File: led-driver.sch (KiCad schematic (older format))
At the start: 18 parts, among them J1 48VDC IN, J2 ENABLE, J3 ADJ, J4 LED, Q1 ZXMP7A17KTC, U1 LM3409HV

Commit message: Rescue symbols, minor revisions to PCB
This commits previous work that took place sporadically between the last
commit a year and a half ago, and now.
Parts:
- C1, C2, C3, C4, C5: symbol C_Small -> led-driver-rescue:C_Small
- D1: symbol D_Schottky_Small_ALT -> led-driver-rescue:D_Schottky_Small_ALT
- J1, J3, J4: symbol CONN_01X02 -> led-driver-rescue:CONN_01X02
- J2: symbol CONN_01X03 -> led-driver-rescue:CONN_01X03
- L1: symbol L_Small -> led-driver-rescue:L_Small
- Q1: symbol Q_PMOS_GDS -> led-driver-rescue:Q_PMOS_GDS
- R1, R2, R3, R4, R5: symbol R_Small -> led-driver-rescue:R_Small
- U1: symbol LM3409-RESCUE-led-driver-new -> led-driver-rescue:LM3409-RESCUE-led-driver-new
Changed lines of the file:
@@
-EESchema Schematic File Version 2
-LIBS:led-driver
-EELAYER 25 0
+EESchema Schematic File Version 4
+LIBS:led-driver-cache
+EELAYER 29 0
 EELAYER END
 $Descr A4 11693 8268
@@
 $EndDescr
 $Comp
-L R_Small R4
+L led-driver-rescue:R_Small R4
 U 1 1 59AE9865
 P 5800 3300
@@
 $EndComp
 $Comp
-L D_Schottky_Small_ALT D1
+L led-driver-rescue:D_Schottky_Small_ALT D1
 U 1 1 59AE99D5
 P 5800 4000
@@
 $EndComp
 $Comp
-L L_Small L1
+L led-driver-rescue:L_Small L1
 U 1 1 59AE9B0A
 P 6050 3850
@@
 $EndComp
 $Comp
-L C_Small C3
+L led-driver-rescue:C_Small C3
 U 1 1 59AE9DC4
 P 5650 2900
@@
 $EndComp
 $Comp
-L C_Small C1
+L led-driver-rescue:C_Small C1
 U 1 1 59AE9F39
 P 2300 3100
@@
 $EndComp
 $Comp
-L GND #PWR01
+L led-driver-rescue:GND #PWR01
 U 1 1 59AEA1C1
 P 5800 4100
@@
 $EndComp
 $Comp
-L CONN_01X02 J4
+L led-driver-rescue:CONN_01X02 J4
 U 1 1 59AEA206
 P 6950 3900
@@
 $EndComp
 $Comp
-L GND #PWR02
+L led-driver-rescue:GND #PWR02
 U 1 1 59AEA35C
 P 6750 4100
@@
 $EndComp
 $Comp
-L GND #PWR03
+L led-driver-rescue:GND #PWR03
 U 1 1 59AEA3BF
 P 4350 3750
@@
 $EndComp
 $Comp
-L C_Small C2
+L led-driver-rescue:C_Small C2
 U 1 1 59AEA43B
 P 4250 4100
@@
 $EndComp
 $Comp
-L R_Small R1
+L led-driver-rescue:R_Small R1
 U 1 1 59AEA5E2
 P 4550 4000
@@
 $EndComp
 $Comp
-L GND #PWR04
+L led-driver-rescue:GND #PWR04
 U 1 1 59AEA82C
 P 4250 4200
@@
 $EndComp
 $Comp
-L GND #PWR05
+L led-driver-rescue:GND #PWR05
 U 1 1 59AEABBE
 P 2300 3200
@@
 $EndComp
 $Comp
-L CONN_01X02 J1
+L led-driver-rescue:CONN_01X02 J1
 U 1 1 59AEAC70
 P 1900 3050
@@
 $EndComp
 $Comp
-L R_Small R3
+L led-driver-rescue:R_Small R3
 U 1 1 59AEAE7C
 P 4100 2500
@@
 $EndComp
 $Comp
-L R_Small R2
+L led-driver-rescue:R_Small R2
 U 1 1 59AEAEBF
 P 4100 2700
@@
 $EndComp
 $Comp
-L VCC #PWR06
+L led-driver-rescue:VCC #PWR06
 U 1 1 59AEAF69
 P 4100 2400
@@
 $EndComp
 $Comp
-L VCC #PWR07
+L led-driver-rescue:VCC #PWR07
 U 1 1 59AEAFA4
 P 5800 3200
@@
 $EndComp
 $Comp
-L VCC #PWR08
+L led-driver-rescue:VCC #PWR08
 U 1 1 59AEB027
 P 5650 2800
@@
 $EndComp
 $Comp
-L VCC #PWR09
+L led-driver-rescue:VCC #PWR09
 U 1 1 59AEB4E1
 P 2100 3000
@@
 $EndComp
 $Comp
-L GND #PWR010
+L led-driver-rescue:GND #PWR010
 U 1 1 59AEB7E3
 P 4100 2800
@@
 $EndComp
 $Comp
-L VCC #PWR011
+L led-driver-rescue:VCC #PWR011
 U 1 1 59AEBCD0
 P 3700 3500
@@
 $EndComp
 $Comp
-L GND #PWR012
+L led-driver-rescue:GND #PWR012
 U 1 1 59AEC65E
 P 3500 3100
@@
 $EndComp
 $Comp
-L CONN_01X02 J3
+L led-driver-rescue:CONN_01X02 J3
 U 1 1 59AEC9E5
 P 3300 3050
@@
 $EndComp
 $Comp
-L CONN_01X03 J2
+L led-driver-rescue:CONN_01X03 J2
 U 1 1 59AED2EC
 P 3500 3600
@@
 $EndComp
 $Comp
-L GND #PWR013
+L led-driver-rescue:GND #PWR013
 U 1 1 59AED340
 P 3700 3700
@@
 $EndComp
 $Comp
-L LM3409-RESCUE-led-driver-new U1
+L led-driver-rescue:LM3409-RESCUE-led-driver-new U1
 U 1 1 59AEF993
 P 4900 3200
@@
 $EndComp
 Wire Wire Line
-	5800 3800 5800 3900
+	5800 3800 5800 3850
 Wire Wire Line
 	5800 3850 5950 3850
@@
 	5500 3000 5650 3000
 Wire Wire Line
-	6150 3850 6750 3850
+	6150 3850 6250 3850
 Wire Wire Line
 	6750 4100 6750 3950
@@
 	4300 2600 4300 2800
 Wire Wire Line
-	3500 3000 4300 3000
-$Comp
-L C_Small C4
+	3500 3000 3900 3000
+$Comp
+L led-driver-rescue:C_Small C4
 U 1 1 59AF72EA
 P 3900 3100
@@
 $EndComp
 $Comp
-L GND #PWR014
+L led-driver-rescue:GND #PWR014
 U 1 1 59AF7850
 P 3900 3200
@@
 Connection ~ 3900 3000
 $Comp
-L C_Small C5
+L led-driver-rescue:C_Small C5
 U 1 1 59AFE85B
 P 6400 3950
@@
 $EndComp
 $Comp
-L GND #PWR015
+L led-driver-rescue:GND #PWR015
 U 1 1 59AFEC38
 P 6400 4050
@@
 	4650 4300 6250 4300
 $Comp
-L GND #PWR016
+L led-driver-rescue:GND #PWR016
 U 1 1 59B109B8
 P 4900 3900
@@
 $EndComp
 $Comp
-L R_Small R5
+L led-driver-rescue:R_Small R5
 U 1 1 59B11505
 P 6200 3300
@@
 Connection ~ 5800 3400
 $Comp
-L Q_PMOS_GDS Q1
+L led-driver-rescue:Q_PMOS_GDS Q1
 U 1 1 59B006E4
 P 5700 3600
@@
 $EndComp
 Wire Wire Line
-	5500 3200 6200 3200
-Wire Wire Line
-	5500 3400 6200 3400
+	5500 3200 5800 3200
+Wire Wire Line
+	5500 3400 5800 3400
+Wire Wire Line
+	5800 3850 5800 3900
+Wire Wire Line
+	3900 3000 4300 3000
+Wire Wire Line
+	6400 3850 6750 3850
+Wire Wire Line
+	5800 3200 6200 3200
+Wire Wire Line
+	5800 3400 6200 3400
 $EndSCHEMATC

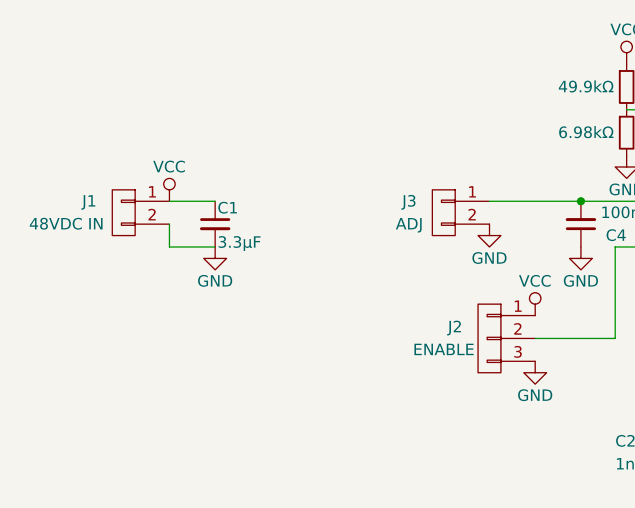
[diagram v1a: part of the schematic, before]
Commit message: Add PWR_FLAGs to power input
This quells warnings about connected-but-not-driven nets for GND and VCC
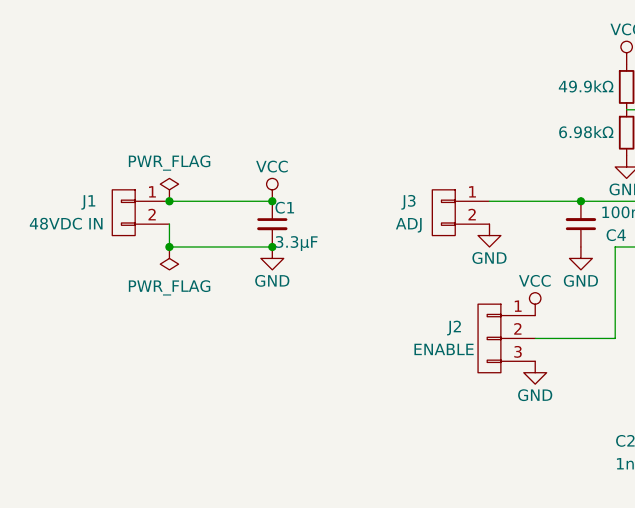
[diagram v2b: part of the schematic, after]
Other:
- moved on the sheet: C1

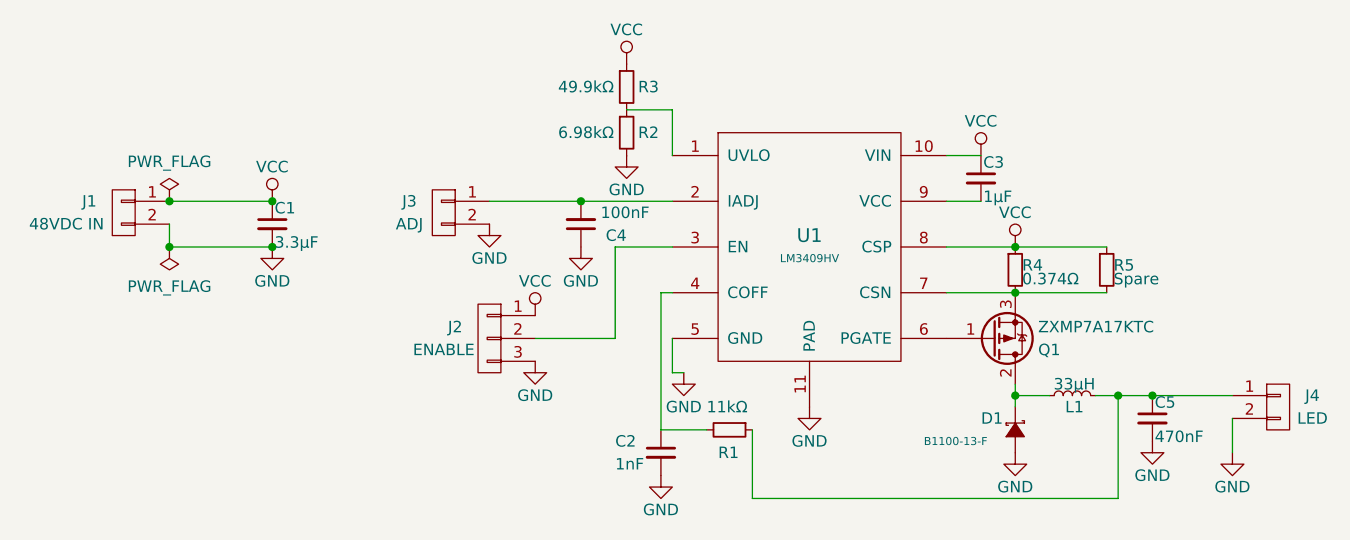
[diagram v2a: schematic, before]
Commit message: Increase UVLO turn-on to 43 V
The initial design assumed that the UVLO was a feature of the LM3409 not needed
by this board. It was set at the datasheet values of 10.1 V turn-on with 1.1 V
of hysteresis. However, during testing, I have found that the supply will sink
a maximum of around 600 mA into the load when operated into dropout. The LM3409
datasheet confirms that this is expected behaviour. Since the supply is
designed for LEDs modules with a forward voltage of 37 V, this patch changes
the UVLO to just over 43 volts, meaning that we do not run the LEDs above the
supply's design current of 450 mA.
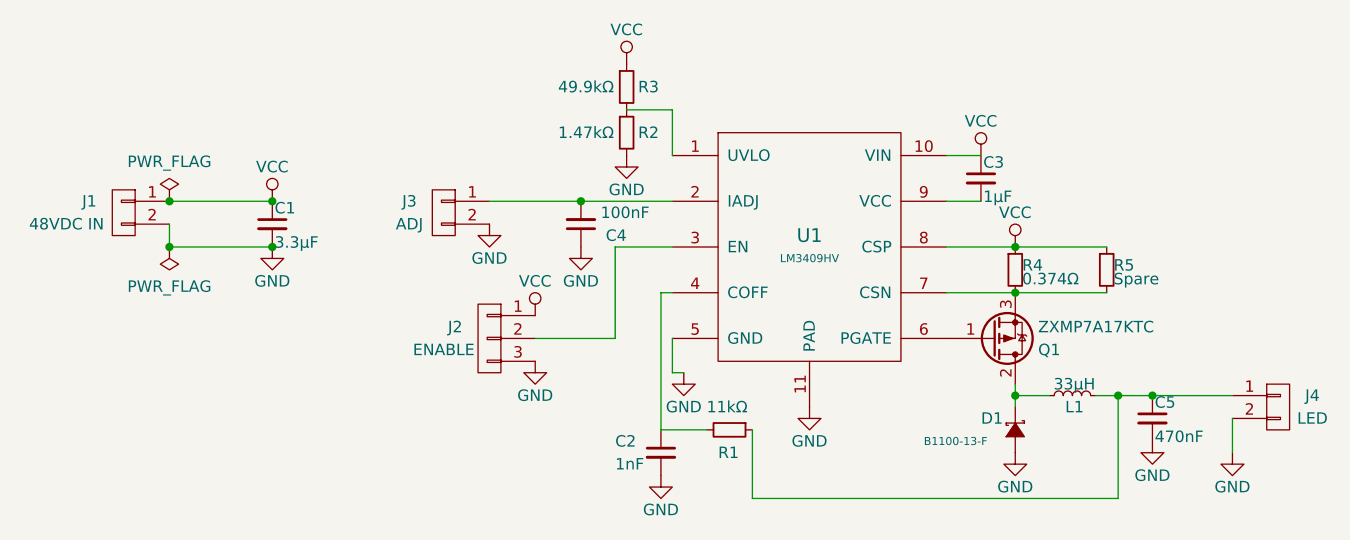
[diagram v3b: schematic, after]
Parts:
- R2: value 6.98kΩ -> 1.47kΩ
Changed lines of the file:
@@
 P 4100 2700
 F 0 "R2" H 4150 2700 50  0000 L CNN
-F 1 "6.98kΩ" H 3800 2700 50  0000 L CNN
+F 1 "1.47kΩ" H 3800 2700 50  0000 L CNN
 F 2 "Resistors_SMD:R_0805" H 4100 2700 50  0001 C CNN
 F 3 "" H 4100 2700 50  0001 C CNN
